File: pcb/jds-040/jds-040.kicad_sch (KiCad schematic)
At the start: 8 parts, among them J1 USB_C_Receptacle_USB2.0, J2 FPC_01x12

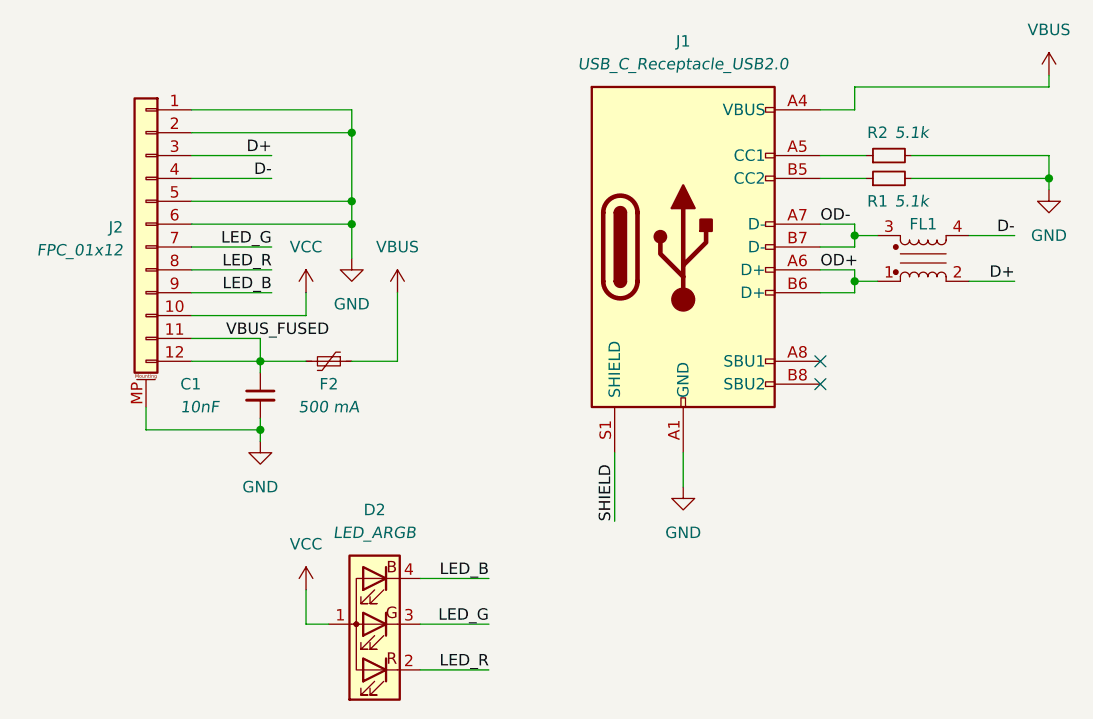
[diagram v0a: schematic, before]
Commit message: Connected shield to ground just like in the original part.
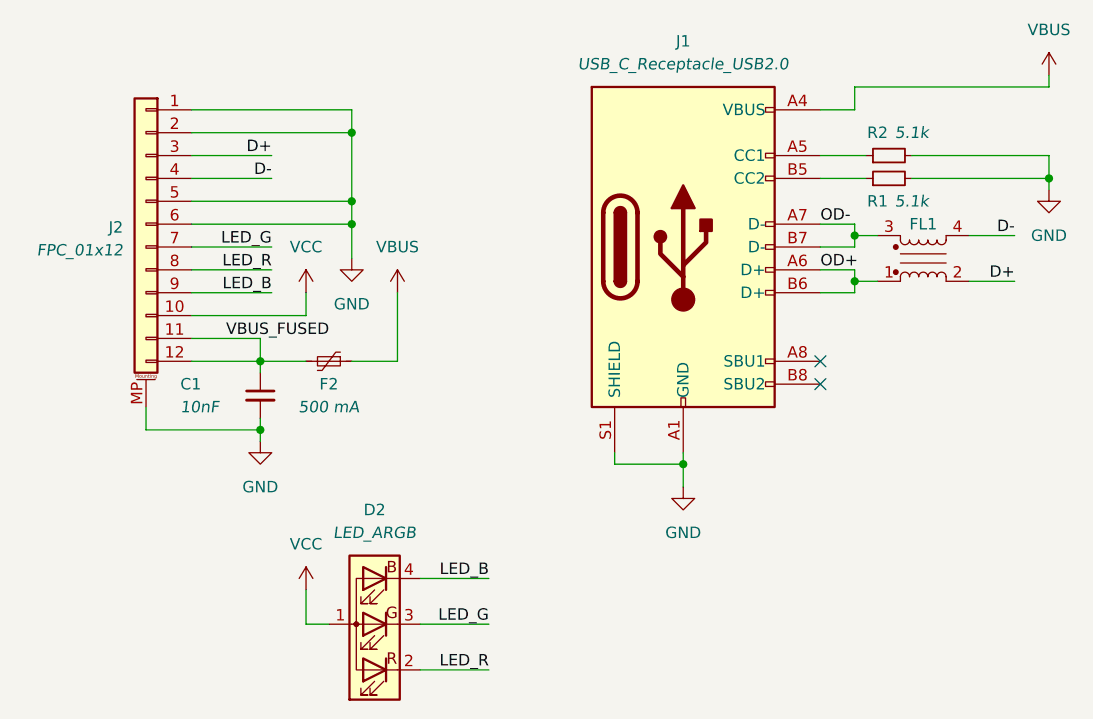
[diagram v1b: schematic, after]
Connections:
- net SHIELD is gone; now on net GND: J1.S1 (SHIELD)
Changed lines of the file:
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@@
   (junction (at 58.42 76.2) (diameter 0) (color 0 0 0 0)
+  )
+  (junction (at 105.41 80.01) (diameter 0) (color 0 0 0 0)
   )
   (junction (at 146.05 48.26) (diameter 0) (color 0 0 0 0)
@@
     (stroke (width 0) (type default))
   )
+  (wire (pts (xy 105.41 80.01) (xy 105.41 82.55))
+    (stroke (width 0) (type default))
+  )
   (wire (pts (xy 124.46 54.61) (xy 127 54.61))
     (stroke (width 0) (type default))
@@
     (stroke (width 0) (type default))
   )
-  (wire (pts (xy 97.79 78.74) (xy 97.79 86.36))
-    (stroke (width 0) (type default))
-  )
   (wire (pts (xy 124.46 40.64) (xy 120.65 40.64))
     (stroke (width 0) (type default))
@@
     (stroke (width 0) (type default))
   )
+  (wire (pts (xy 97.79 78.74) (xy 97.79 80.01))
+    (stroke (width 0) (type default))
+  )
   (wire (pts (xy 124.46 53.34) (xy 124.46 54.61))
     (stroke (width 0) (type default))
@@
     (stroke (width 0) (type default))
   )
-  (wire (pts (xy 105.41 78.74) (xy 105.41 82.55))
+  (wire (pts (xy 105.41 78.74) (xy 105.41 80.01))
     (stroke (width 0) (type default))
   )
@@
   )
   (wire (pts (xy 63.5 93.98) (xy 63.5 97.79))
+    (stroke (width 0) (type default))
+  )
+  (wire (pts (xy 97.79 80.01) (xy 105.41 80.01))
     (stroke (width 0) (type default))
   )
@@
     (effects (font (size 1.27 1.27)) (justify right bottom))
   )
-  (label "SHIELD" (at 97.79 86.36 90) (fields_autoplaced)
-    (effects (font (size 1.27 1.27)) (justify left bottom))
-  )
   (label "LED_G" (at 83.82 97.79 180) (fields_autoplaced)

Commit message: Replaced fuse with a part that satisfies DS4 current rating, upgraded project to Kicad 8
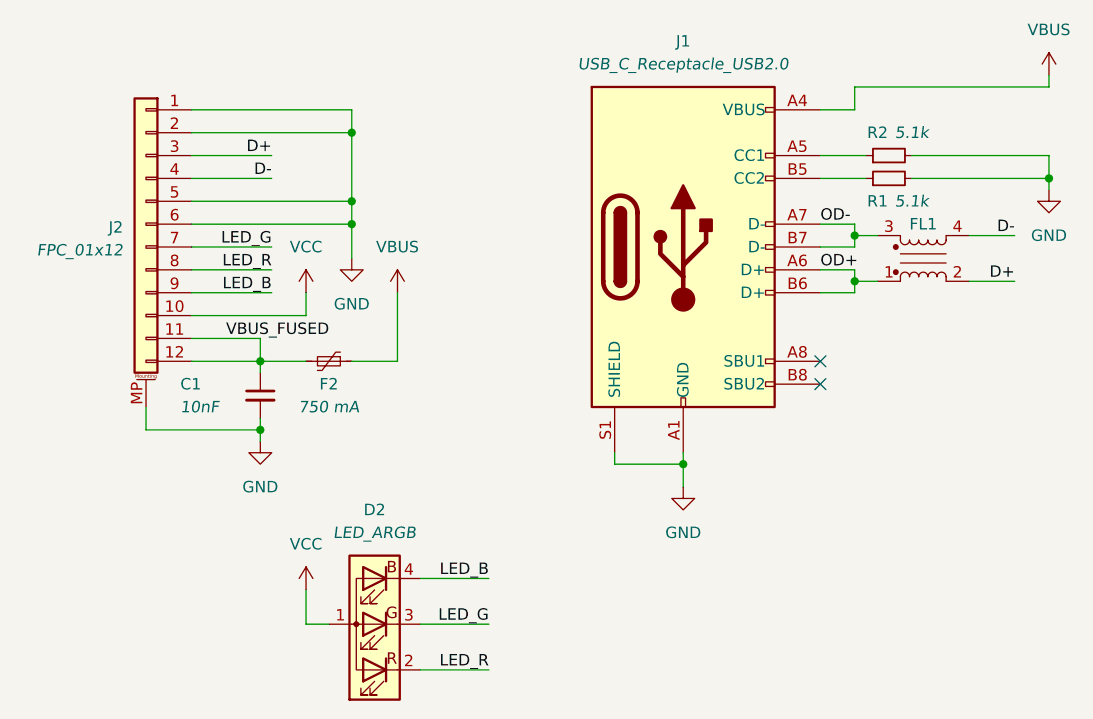
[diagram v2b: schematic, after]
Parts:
- F2: value 500 mA -> 750 mA; LCSC C210356 -> C207016
- FL1: LCSC C383353 -> C383353
- J2: LCSC C466532 -> C466532

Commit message: Changed F2,D2 to F1,D1
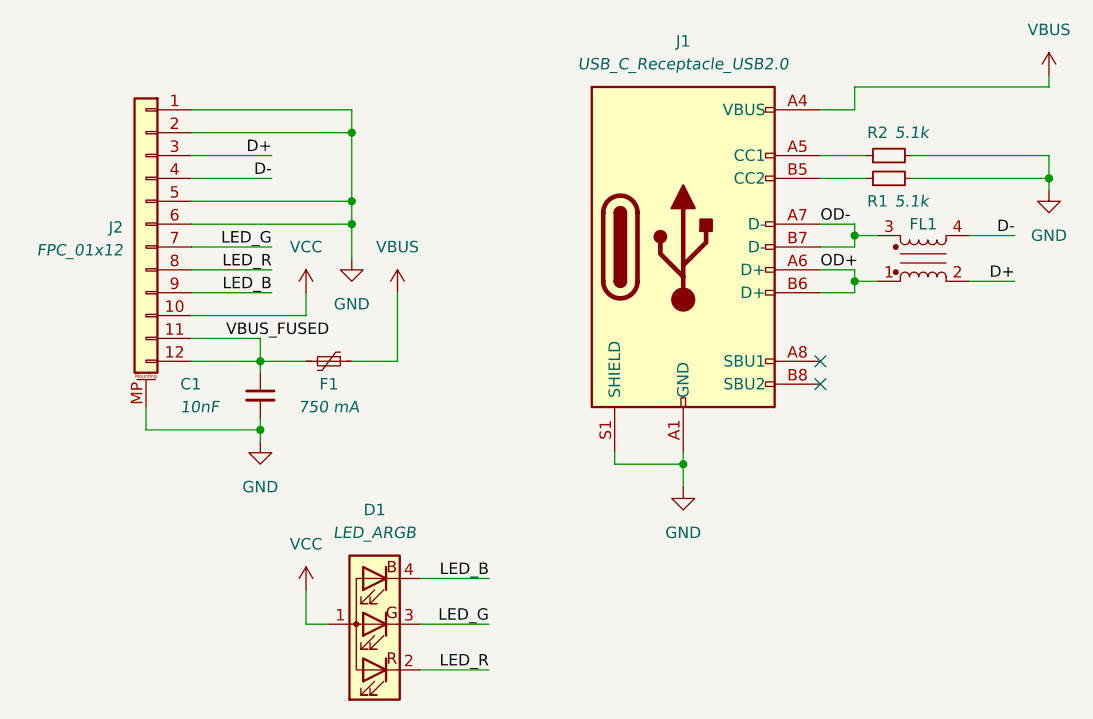
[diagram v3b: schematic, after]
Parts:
- renumbered D2 to D1, F2 to F1
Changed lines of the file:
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@@
 		(on_board yes)
 		(dnp no)
-		(property "Reference" "F2"
+		(property "Reference" "F1"
 			(at 66.04 71.12 90)
 			(effects
@@
 			(project "jds-040"
 				(path "/6878427b-1c14-4846-8103-c4c03da88062"
-					(reference "F2")
+					(reference "F1")
 					(unit 1)
 				)
@@
 		(dnp no)
 		(fields_autoplaced yes)
-		(property "Reference" "D2"
+		(property "Reference" "D1"
 			(at 71.12 85.09 0)
 			(effects
@@
 			(project "jds-040"
 				(path "/6878427b-1c14-4846-8103-c4c03da88062"
-					(reference "D2")
-					(unit 1)
-				)
+					(reference "D1")
+					(unit 1)
+				)
